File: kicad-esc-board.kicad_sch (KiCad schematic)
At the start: 0 parts

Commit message: Added schematic, board, footprints, symbols, and models for rough draft
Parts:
- added H1, H2: MountingHole_Pad, MountingHole:MountingHole_3.2mm_M3_Pad, symbol Mechanical:MountingHole_Pad
- added HS1: Heatsink_Pad, esc_board_custom_footprints:ESC_HeatSink, symbol Mechanical:Heatsink_Pad
- added J1: PhoenixContact_01x03_WireToBoard_TerminalBlock, esc_board_custom_footprints:CONN_1017492, symbol esc_board_custom_symbols:PhoenixContact_01x03_WireToBoard_TerminalBlock
- added J2: PhoenixContact_01x02_WireToBoard_TerminalBlock, esc_board_custom_footprints:CONN_1017491, symbol esc_board_custom_symbols:PhoenixContact_01x02_WireToBoard_TerminalBlock
- added J4: JST_01x02_TH_Vertical, esc_board_custom_footprints:JST_B2B-PH-K-S, symbol esc_board_custom_symbols:JST_01x02_TH_Vertical
- added M1: Blue Robotics Basic ESC, esc_board_custom_footprints:BlueRobotics_ESC_Basic, symbol esc_board_custom_symbols:ESC
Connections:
- new net: J1.1 (Pin_1), M1.3 (Signal-1)
- new net: J1.2 (Pin_2), M1.4 (Signal-2)
- new net: J1.3 (Pin_3), M1.5 (Signal-3)
- new net: J2.1 (Pin_1), M1.1 (V_BATT)
- new net: J4.1 (Pin_1), M1.6 (PWM-Ctrl)
- new net: J4.2 (Pin_2), M1.7 (PWM-GND)
- new net GND: H1.1, H2.1, HS1.1, J2.2 (Pin_2), M1.2 (GND), M1.8 (HEAT-SINK)

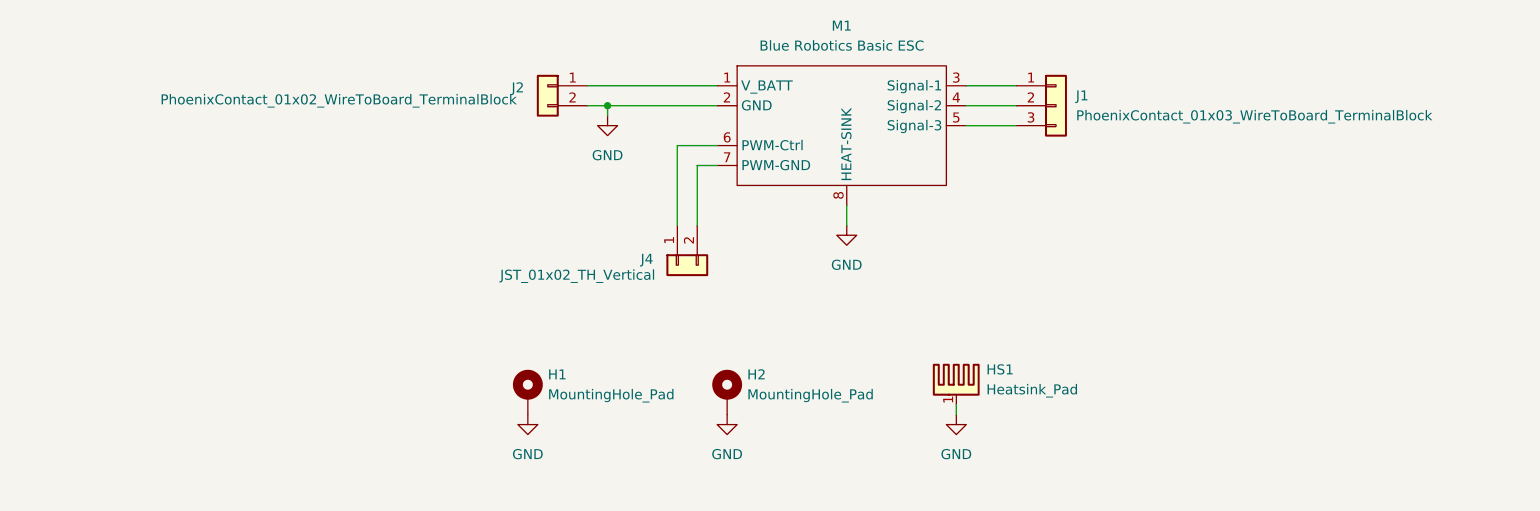
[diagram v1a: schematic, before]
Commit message: Updated to w/ JST
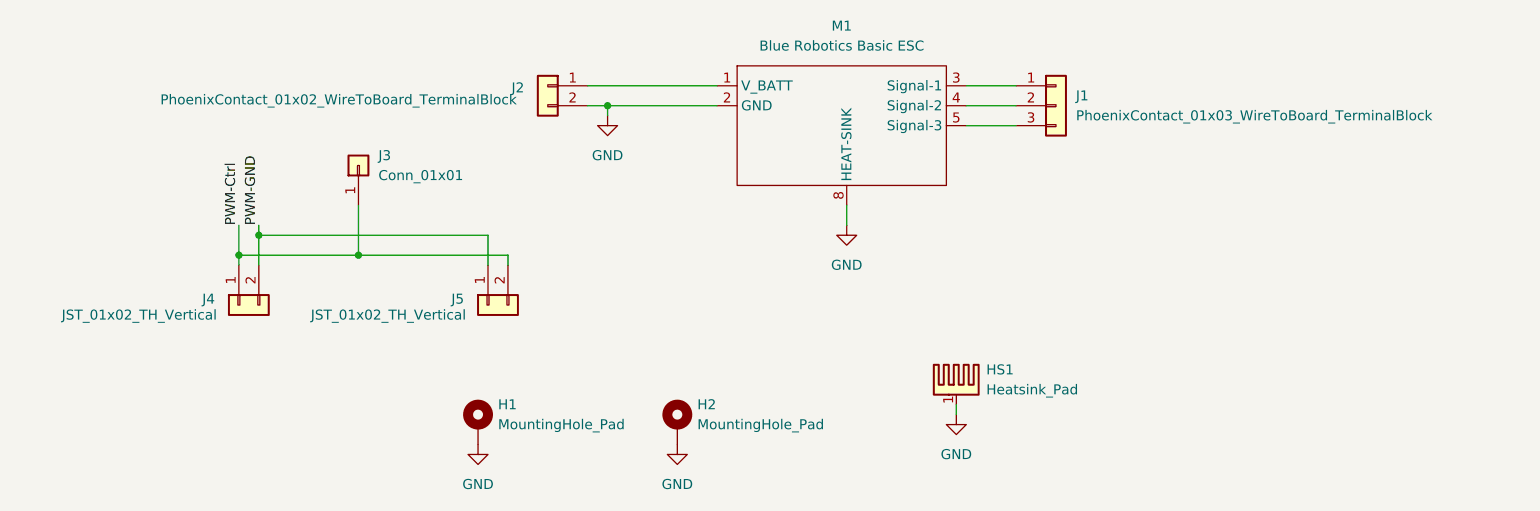
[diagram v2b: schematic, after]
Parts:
- added J3: Conn_01x01, Connector_PinHeader_2.54mm:PinHeader_1x01_P2.54mm_Vertical, symbol Connector_Generic:Conn_01x01
- added J5: JST_01x02_TH_Vertical, esc_board_custom_footprints:JST_B2B-PH-K-S, symbol esc_board_custom_symbols:JST_01x02_TH_Vertical
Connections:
- net PWM-Ctrl: now reaches J4.1 (Pin_1)
- net PWM-Ctrl: now also J3.1 (Pin_1), J5.2 (Pin_2); no longer M1.6 (PWM-Ctrl)
- net PWM-GND: now reaches J4.2 (Pin_2)
- net PWM-GND: now also J5.1 (Pin_1); no longer M1.7 (PWM-GND)
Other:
- moved on the sheet: H1, H2, J4
